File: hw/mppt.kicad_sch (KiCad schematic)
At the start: 4 parts

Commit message: savestate layout
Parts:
- added JP101, JP102, JP103, JP104, JP105: SolderJumper_2_Open, symbol Jumper:SolderJumper_2_Open
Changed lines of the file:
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@@
     (effects (font (size 1.27 1.27)) (justify left bottom))
   )
+  (symbol (lib_id "Jumper:SolderJumper_2_Open") (at 74.93 160.02 0) (unit 1)
+    (in_bom yes) (on_board yes) (dnp no) (fields_autoplaced)
+    (property "Reference" "JP104" (at 74.93 154.94 0)
+      (effects (font (size 1.27 1.27)))
+    )
+    (property "Value" "SolderJumper_2_Open" (at 74.93 157.48 0)
+      (effects (font (size 1.27 1.27)))
+    )
+    (property "Footprint" "" (at 74.93 160.02 0)
+      (effects (font (size 1.27 1.27)) hide)
+    )
+    (property "Datasheet" "~" (at 74.93 160.02 0)
+      (effects (font (size 1.27 1.27)) hide)
+    )
+    (pin "1")
+    (pin "2")
+    (instances
+      (project "mppt"
+        (path "/06fd3a42-664d-41bc-bf0f-b5ee0ddcc902"
+          (reference "JP104") (unit 1)
+        )
+      )
+    )
+  )
   (symbol (lib_id "Mechanical:MountingHole") (at 36.83 101.6 0) (unit 1)
     (in_bom yes) (on_board yes) (dnp no)
@@
     )
   )
+  (symbol (lib_id "Jumper:SolderJumper_2_Open") (at 74.93 142.24 0) (unit 1)
+    (in_bom yes) (on_board yes) (dnp no) (fields_autoplaced)
+    (property "Reference" "JP102" (at 74.93 137.16 0)
+      (effects (font (size 1.27 1.27)))
+    )
+    (property "Value" "SolderJumper_2_Open" (at 74.93 139.7 0)
+      (effects (font (size 1.27 1.27)))
+    )
+    (property "Footprint" "" (at 74.93 142.24 0)
+      (effects (font (size 1.27 1.27)) hide)
+    )
+    (property "Datasheet" "~" (at 74.93 142.24 0)
+      (effects (font (size 1.27 1.27)) hide)
+    )
+    (pin "1")
+    (pin "2")
+    (instances
+      (project "mppt"
+        (path "/06fd3a42-664d-41bc-bf0f-b5ee0ddcc902"
+          (reference "JP102") (unit 1)
+        )
+      )
+    )
+  )
+  (symbol (lib_id "Jumper:SolderJumper_2_Open") (at 74.93 168.91 0) (unit 1)
+    (in_bom yes) (on_board yes) (dnp no) (fields_autoplaced)
+    (property "Reference" "JP105" (at 74.93 163.83 0)
+      (effects (font (size 1.27 1.27)))
+    )
+    (property "Value" "SolderJumper_2_Open" (at 74.93 166.37 0)
+      (effects (font (size 1.27 1.27)))
+    )
+    (property "Footprint" "" (at 74.93 168.91 0)
+      (effects (font (size 1.27 1.27)) hide)
+    )
+    (property "Datasheet" "~" (at 74.93 168.91 0)
+      (effects (font (size 1.27 1.27)) hide)
+    )
+    (pin "1")
+    (pin "2")
+    (instances
+      (project "mppt"
+        (path "/06fd3a42-664d-41bc-bf0f-b5ee0ddcc902"
+          (reference "JP105") (unit 1)
+        )
+      )
+    )
+  )
   (symbol (lib_id "Mechanical:MountingHole") (at 36.83 106.68 0) (unit 1)
     (in_bom yes) (on_board yes) (dnp no)
@@
     )
   )
+  (symbol (lib_id "Jumper:SolderJumper_2_Open") (at 74.93 133.35 0) (unit 1)
+    (in_bom yes) (on_board yes) (dnp no) (fields_autoplaced)
+    (property "Reference" "JP101" (at 74.93 128.27 0)
+      (effects (font (size 1.27 1.27)))
+    )
+    (property "Value" "SolderJumper_2_Open" (at 74.93 130.81 0)
+      (effects (font (size 1.27 1.27)))
+    )
+    (property "Footprint" "" (at 74.93 133.35 0)
+      (effects (font (size 1.27 1.27)) hide)
+    )
+    (property "Datasheet" "~" (at 74.93 133.35 0)
+      (effects (font (size 1.27 1.27)) hide)
+    )
+    (pin "1")
+    (pin "2")
+    (instances
+      (project "mppt"
+        (path "/06fd3a42-664d-41bc-bf0f-b5ee0ddcc902"
+          (reference "JP101") (unit 1)
+        )
+      )
+    )
+  )
   (symbol (lib_id "Mechanical:MountingHole") (at 36.83 116.84 0) (unit 1)
     (in_bom yes) (on_board yes) (dnp no)
@@
         )
       )
+    )
+  )
+  (symbol (lib_id "Jumper:SolderJumper_2_Open") (at 74.93 151.13 0) (unit 1)
+    (in_bom yes) (on_board yes) (dnp no) (fields_autoplaced)
+    (property "Reference" "JP103" (at 74.93 146.05 0)
+      (effects (font (size 1.27 1.27)))
+    )
+    (property "Value" "SolderJumper_2_Open" (at 74.93 148.59 0)
+      (effects (font (size 1.27 1.27)))
+    )
+    (property "Footprint" "" (at 74.93 151.13 0)
+      (effects (font (size 1.27 1.27)) hide)
+    )
+    (property "Datasheet" "~" (at 74.93 151.13 0)
+      (effects (font (size 1.27 1.27)) hide)
+    )
+    (pin "1")
+    (pin "2")
+    (instances
+      (project "mppt"
+        (path "/06fd3a42-664d-41bc-bf0f-b5ee0ddcc902"
+          (reference "JP103") (unit 1)
+        )
+      )

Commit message: final layout
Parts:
- removed JP101, JP102, JP103, JP104, JP105: SolderJumper_2_Open, symbol Jumper:SolderJumper_2_Open
- added TJ302, TJ303 (x2): Thermal Jumper, mppt:1225_SMD, symbol Jumper:SolderJumper_2_Bridged
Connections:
- net V_ARR+: now also TJ303.2 (B)
- net V_BATT+: now also TJ303.2 (B)
- net V_SW: now also TJ302.1 (A), TJ303.1 (A), TJ303.1 (A)
- new net +12V: TJ302.2 (B)

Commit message: temp for matthew to stitch
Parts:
- added TJ302: Thermal Jumper, Resistor_SMD:R_0805_2012Metric, symbol Jumper:SolderJumper_2_Bridged
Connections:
- net +12V: now also TJ302.1 (A)
- net V_BATT+: now also TJ302.2 (B)
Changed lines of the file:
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@@
+    (stroke (width 0) (type default))
+  )
+  (wire (pts (xy 61.595 157.48) (xy 64.77 157.48))
     (stroke (width 0) (type default))
   )
@@
   )
   (label "V_SW" (at 125.73 57.15 0) (fields_autoplaced)
+    (effects (font (size 1.27 1.27)) (justify left bottom))
+  )
+  (label "V_BATT+" (at 72.39 157.48 0) (fields_autoplaced)
     (effects (font (size 1.27 1.27)) (justify left bottom))
   )
@@
     )
   )
+  (symbol (lib_id "power:+12V") (at 61.595 157.48 0) (unit 1)
+    (in_bom yes) (on_board yes) (dnp no) (fields_autoplaced)
+    (property "Reference" "#PWR0206" (at 61.595 161.29 0)
+      (effects (font (size 1.27 1.27)) hide)
+    )
+    (property "Value" "+12V" (at 61.595 153.67 0)
+      (effects (font (size 1.27 1.27)))
+    )
+    (property "Footprint" "" (at 61.595 157.48 0)
+      (effects (font (size 1.27 1.27)) hide)
+    )
+    (property "Datasheet" "" (at 61.595 157.48 0)
+      (effects (font (size 1.27 1.27)) hide)
+    )
+    (pin "1")
+    (instances
+      (project "mppt"
+        (path "/06fd3a42-664d-41bc-bf0f-b5ee0ddcc902/90f57858-b3ac-468b-8edb-acb0ab266950"
+          (reference "#PWR0206") (unit 1)
+        )
+        (path "/06fd3a42-664d-41bc-bf0f-b5ee0ddcc902"
+          (reference "#PWR01") (unit 1)
+        )
+      )
+    )
+  )
   (symbol (lib_id "Mechanical:MountingHole") (at 36.83 106.68 0) (unit 1)
     (in_bom yes) (on_board yes) (dnp no)
@@
         )
       )
+    )
+  )
+  (symbol (lib_id "Jumper:SolderJumper_2_Bridged") (at 68.58 157.48 0) (unit 1)
+    (in_bom yes) (on_board yes) (dnp no)
+    (property "Reference" "TJ302" (at 71.12 154.94 0)
+      (effects (font (size 1.27 1.27)) (justify right))
+    )
+    (property "Value" "Thermal Jumper" (at 74.93 160.02 0)
+      (effects (font (size 1.27 1.27)) (justify right) hide)
+    )
+    (property "Footprint" "Resistor_SMD:R_0805_2012Metric" (at 68.58 157.48 0)
+      (effects (font (size 1.27 1.27)) hide)
+    )
+    (property "Datasheet" "https://media.digikey.com/pdf/Data%20Sheets/AVX%20PDFs/Q-Bridge_Series.pdf" (at 68.58 157.48 0)
+      (effects (font (size 1.27 1.27)) hide)
+    )
+    (property "Distributor" "Digikey" (at 68.58 157.48 0)
+      (effects (font (size 1.27 1.27)) hide)
+    )
+    (property "Manufacturer" "Kyocera AVX" (at 68.58 157.48 0)
+      (effects (font (size 1.27 1.27)) hide)
+    )
+    (property "P/N" "QB0805B40WYT" (at 68.58 157.48 0)
+      (effects (font (size 1.27 1.27)) hide)
+    )
+    (pin "1")
+    (pin "2")
+    (instances
+      (project "mppt"
+        (path "/06fd3a42-664d-41bc-bf0f-b5ee0ddcc902/9cd55a57-0ec8-481d-b571-b5fdbe353ce7"
+          (reference "TJ302") (unit 1)
+        )
+        (path "/06fd3a42-664d-41bc-bf0f-b5ee0ddcc902"
+          (reference "TJ104") (unit 1)
+        )
+      )
+      (project "irradiance1"
+        (path "/6d1e098a-11c7-4ba2-9d1b-897fdadef7a1"
+          (reference "TJ105") (unit 1)
+        )
+      )

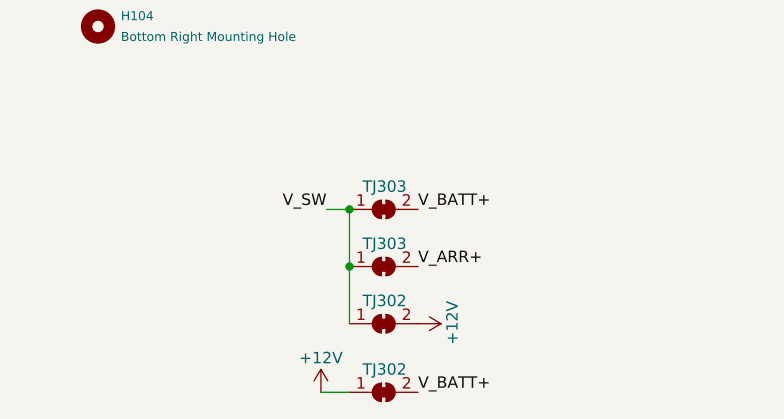
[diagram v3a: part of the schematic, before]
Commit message: production files for v0.1.0. Change cap power calc to be based off i_rms of i_pkpk, not i_pk + r_l_a
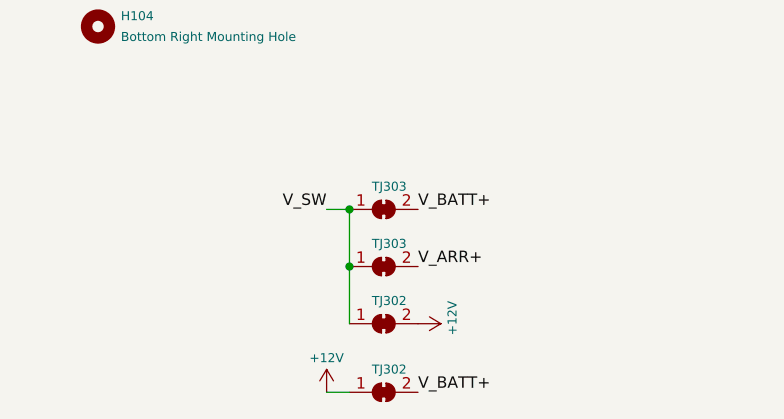
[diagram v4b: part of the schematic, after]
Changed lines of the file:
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@@
     (stroke (width 0) (type default))
   )
-  (wire (pts (xy 61.595 157.48) (xy 64.77 157.48))
+  (wire (pts (xy 62.23 157.48) (xy 64.77 157.48))
     (stroke (width 0) (type default))
   )
@@
     (in_bom yes) (on_board yes) (dnp no)
     (property "Reference" "#PWR0101" (at 68.58 149.86 0)
-      (effects (font (size 1.27 1.27)) hide)
+      (effects (font (size 1 1)) hide)
     )
     (property "Value" "+12V" (at 76.2 147.32 0)
-      (effects (font (size 1.27 1.27)) (justify left))
+      (effects (font (size 1 1)) (justify left))
     )
     (property "Footprint" "" (at 72.39 149.86 0)
@@
       (effects (font (size 1.27 1.27)) hide)
     )
+    (property "LCSC Part #" "" (at 36.83 101.6 0)
+      (effects (font (size 1.27 1.27)) hide)
+    )
     (instances
       (project "mppt"
@@
       (effects (font (size 1.27 1.27)) hide)
     )
+    (property "LCSC Part #" "" (at 36.83 111.76 0)
+      (effects (font (size 1.27 1.27)) hide)
+    )
     (instances
       (project "mppt"
@@
     )
   )
-  (symbol (lib_id "power:+12V") (at 61.595 157.48 0) (unit 1)
+  (symbol (lib_id "power:+12V") (at 62.23 157.48 0) (unit 1)
     (in_bom yes) (on_board yes) (dnp no) (fields_autoplaced)
-    (property "Reference" "#PWR0206" (at 61.595 161.29 0)
-      (effects (font (size 1.27 1.27)) hide)
-    )
-    (property "Value" "+12V" (at 61.595 153.67 0)
-      (effects (font (size 1.27 1.27)))
-    )
-    (property "Footprint" "" (at 61.595 157.48 0)
-      (effects (font (size 1.27 1.27)) hide)
-    )
-    (property "Datasheet" "" (at 61.595 157.48 0)
+    (property "Reference" "#PWR0206" (at 62.23 161.29 0)
+      (effects (font (size 1 1)) hide)
+    )
+    (property "Value" "+12V" (at 62.23 153.67 0)
+      (effects (font (size 1 1)))
+    )
+    (property "Footprint" "" (at 62.23 157.48 0)
+      (effects (font (size 1.27 1.27)) hide)
+    )
+    (property "Datasheet" "" (at 62.23 157.48 0)
       (effects (font (size 1.27 1.27)) hide)
     )
@@
     )
     (property "P/N" "" (at 36.83 106.68 0)
+      (effects (font (size 1.27 1.27)) hide)
+    )
+    (property "LCSC Part #" "" (at 36.83 106.68 0)
       (effects (font (size 1.27 1.27)) hide)
     )
@@
     (in_bom yes) (on_board yes) (dnp no)
     (property "Reference" "TJ303" (at 71.12 140.97 0)
-      (effects (font (size 1.27 1.27)) (justify right))
+      (effects (font (size 1 1)) (justify right))
     )
     (property "Value" "Thermal Jumper" (at 74.93 146.05 0)
-      (effects (font (size 1.27 1.27)) (justify right) hide)
+      (effects (font (size 1 1)) (justify right) hide)
     )
     (property "Footprint" "mppt:1225_SMD" (at 68.58 143.51 0)
@@
     )
     (property "P/N" "THJP1225AST1" (at 68.58 143.51 0)
+      (effects (font (size 1.27 1.27)) hide)
+    )
+    (property "LCSC Part #" "" (at 68.58 143.51 0)
       (effects (font (size 1.27 1.27)) hide)
     )
@@
     (in_bom yes) (on_board yes) (dnp no)
     (property "Reference" "TJ302" (at 71.12 147.32 0)
-      (effects (font (size 1.27 1.27)) (justify right))
+      (effects (font (size 1 1)) (justify right))
     )
     (property "Value" "Thermal Jumper" (at 74.93 152.4 0)
-      (effects (font (size 1.27 1.27)) (justify right) hide)
+      (effects (font (size 1 1)) (justify right) hide)
     )
     (property "Footprint" "mppt:1225_SMD" (at 68.58 149.86 0)
@@
     )
     (property "P/N" "THJP1225AST1" (at 68.58 149.86 0)
+      (effects (font (size 1.27 1.27)) hide)
+    )
+    (property "LCSC Part #" "" (at 68.58 149.86 0)
       (effects (font (size 1.27 1.27)) hide)
     )
@@
       (effects (font (size 1.27 1.27)) hide)
     )
+    (property "LCSC Part #" "" (at 36.83 116.84 0)
+      (effects (font (size 1.27 1.27)) hide)
+    )
     (instances
       (project "mppt"
@@
     (in_bom yes) (on_board yes) (dnp no)
     (property "Reference" "TJ302" (at 71.12 154.94 0)
-      (effects (font (size 1.27 1.27)) (justify right))
+      (effects (font (size 1 1)) (justify right))
     )
     (property "Value" "Thermal Jumper" (at 74.93 160.02 0)
-      (effects (font (size 1.27 1.27)) (justify right) hide)
+      (effects (font (size 1 1)) (justify right) hide)
     )
     (property "Footprint" "Resistor_SMD:R_0805_2012Metric" (at 68.58 157.48 0)
@@
     )
     (property "P/N" "QB0805B40WYT" (at 68.58 157.48 0)
+      (effects (font (size 1.27 1.27)) hide)
+    )
+    (property "LCSC Part #" "" (at 68.58 157.48 0)
       (effects (font (size 1.27 1.27)) hide)
     )
@@
     (in_bom yes) (on_board yes) (dnp no)
     (property "Reference" "TJ303" (at 71.12 134.62 0)
-      (effects (font (size 1.27 1.27)) (justify right))
+      (effects (font (size 1 1)) (justify right))
     )
     (property "Value" "Thermal Jumper" (at 74.93 139.7 0)
-      (effects (font (size 1.27 1.27)) (justify right) hide)
+      (effects (font (size 1 1)) (justify right) hide)
     )
     (property "Footprint" "mppt:1225_SMD" (at 68.58 137.16 0)
@@
       (effects (font (size 1.27 1.27)) hide)
     )
+    (property "LCSC Part #" "" (at 68.58 137.16 0)
+      (effects (font (size 1.27 1.27)) hide)
+    )

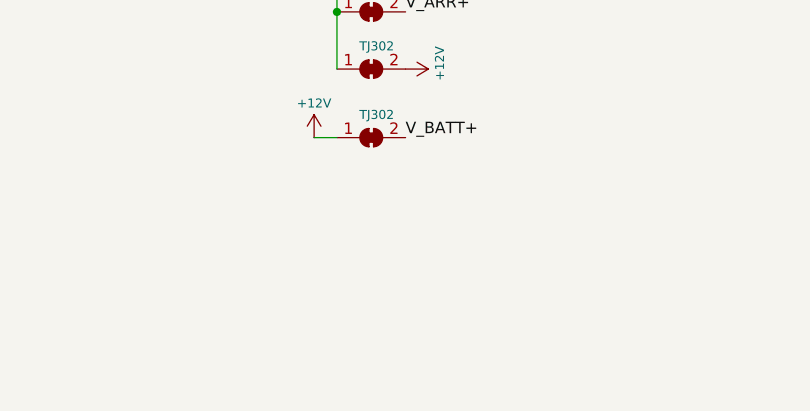
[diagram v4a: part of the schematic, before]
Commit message: added TJ's and 15uF output capacitor population options
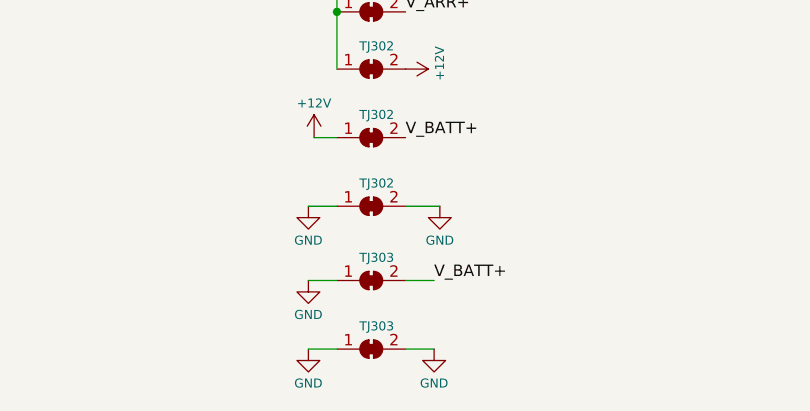
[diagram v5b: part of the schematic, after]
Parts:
- added TJ302: Thermal Jumper, Resistor_SMD:R_0805_2012Metric, symbol Jumper:SolderJumper_2_Bridged
- added TJ303 (x2): Thermal Jumper, mppt:1225_SMD, symbol Jumper:SolderJumper_2_Bridged
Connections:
- net V_BATT+: now also TJ303.2 (B)
- new net GND: TJ302.1 (A), TJ302.2 (B), TJ303.1 (A), TJ303.1 (A), TJ303.2 (B)
